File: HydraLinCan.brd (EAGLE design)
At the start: 59.9 x 37 mm, 33 parts, among them CN1 8p-2.54, J1 HYDRABUS_SHIELD_CON_HEADER_2X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, J2 HYDRABUS_SHIELD_CON_HEADER_2X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, J3 HYDRABUS_SHIELD_CON_HEADER_2X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, K1 TS-1188E, U1 SN65HVD233DG4, U2 SN65HVD233DG4, U3 CJ78M05-to252

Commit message: 2 layers parts
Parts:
- moved R5 18.7 mm to (10.2, 24.1), flipped to the bottom
- moved R2 18.4 mm to (14.5, 22.4), turned to 180 degrees
- moved C11 15.8 mm to (19.6, 32.4), flipped to the bottom, turned to 90 degrees
- moved C5 14.5 mm to (10.4, 14.7), flipped to the bottom, turned to 0 degrees
- moved R4 13.7 mm to (10.5, 10.5), flipped to the bottom, turned to 0 degrees
- moved R11 11.0 mm to (48.9, 19.8), turned to 270 degrees
- moved CAN1 10.4 mm to (26.8, 14.4), turned to 270 degrees
- moved R3 9.83 mm to (27.9, 10.0), flipped to the bottom, turned to 180 degrees
- moved R10 9.63 mm to (49.0, 11.4), turned to 270 degrees
- moved R9 9.22 mm to (26.5, 23.5), turned to 180 degrees
- moved J_USB 8.96 mm to (15.1, 3.81)
- moved R6 8.81 mm to (37.0, 14.4), flipped to the bottom, turned to 270 degrees
- moved R8 8.72 mm to (26.7, 10.9), turned to 0 degrees
- moved C12 8.58 mm to (15.2, 18.0), flipped to the bottom, turned to 0 degrees
- moved C10 7.27 mm to (25.7, 23.5), flipped to the bottom, turned to 180 degrees
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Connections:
- net N$10 renamed CAN1_P
- net N$11 renamed CAN2_N
- net N$12 renamed CAN2_P
- net N$9 renamed CAN1_N
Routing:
- net +3V3: track 77.6 -> 123.1 mm, vias 5 -> 4
- net N$1: track 48.5 -> 19.9 mm, vias 2 -> 0
- net N$4: track 46.5 -> 19.3 mm, vias 2 -> 0
- net N$17: track 47.4 -> 21.3 mm, vias 4 -> 0
- net GND: track 41.7 -> 62.3 mm, vias 11 -> 5
- net N$13: track 57.3 -> 37.1 mm, vias 3 -> 2
- net CAN1_N: track 56.9 -> 36.7 mm
- net N$15: track 42.1 -> 60.9 mm, vias 2 -> 0
- net N$21: track 32.7 -> 16.5 mm, vias 3 -> 0
- net N$19: track 20.4 -> 4.43 mm, vias 3 -> 0
- net PA10: track 41.9 -> 57.1 mm, vias 4 -> 0
- net N$16: track 17.6 -> 5.60 mm
- net PB7: track 14.4 -> 4.26 mm, vias 2 -> 0
- net PB5: track 13.1 -> 23.0 mm
- net PA2: track 30.1 -> 20.3 mm, vias 4 -> 0
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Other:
- board text added: "HydraLINCAN 1.2"
- board text removed: "HydraCANLIN Shield 1_1"

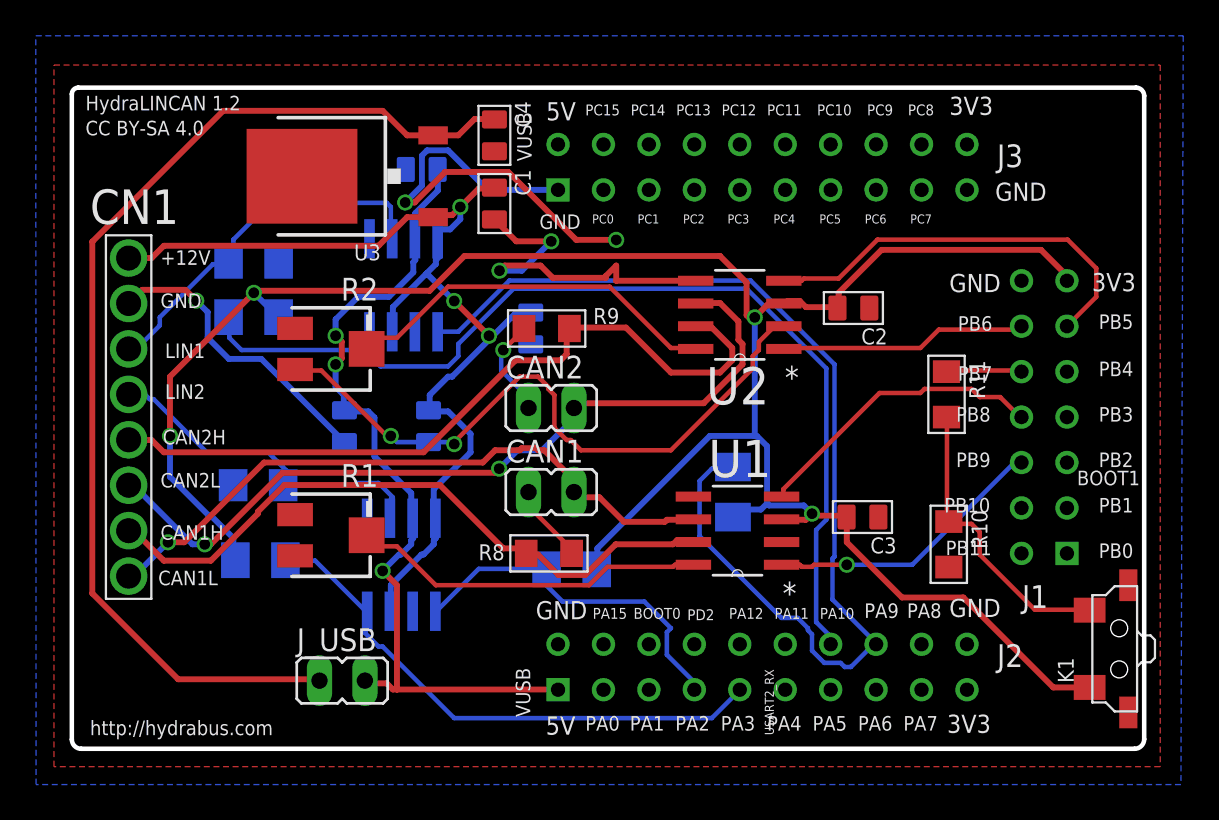
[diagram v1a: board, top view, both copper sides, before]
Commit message: Routing CAN H/L as real diff pairs
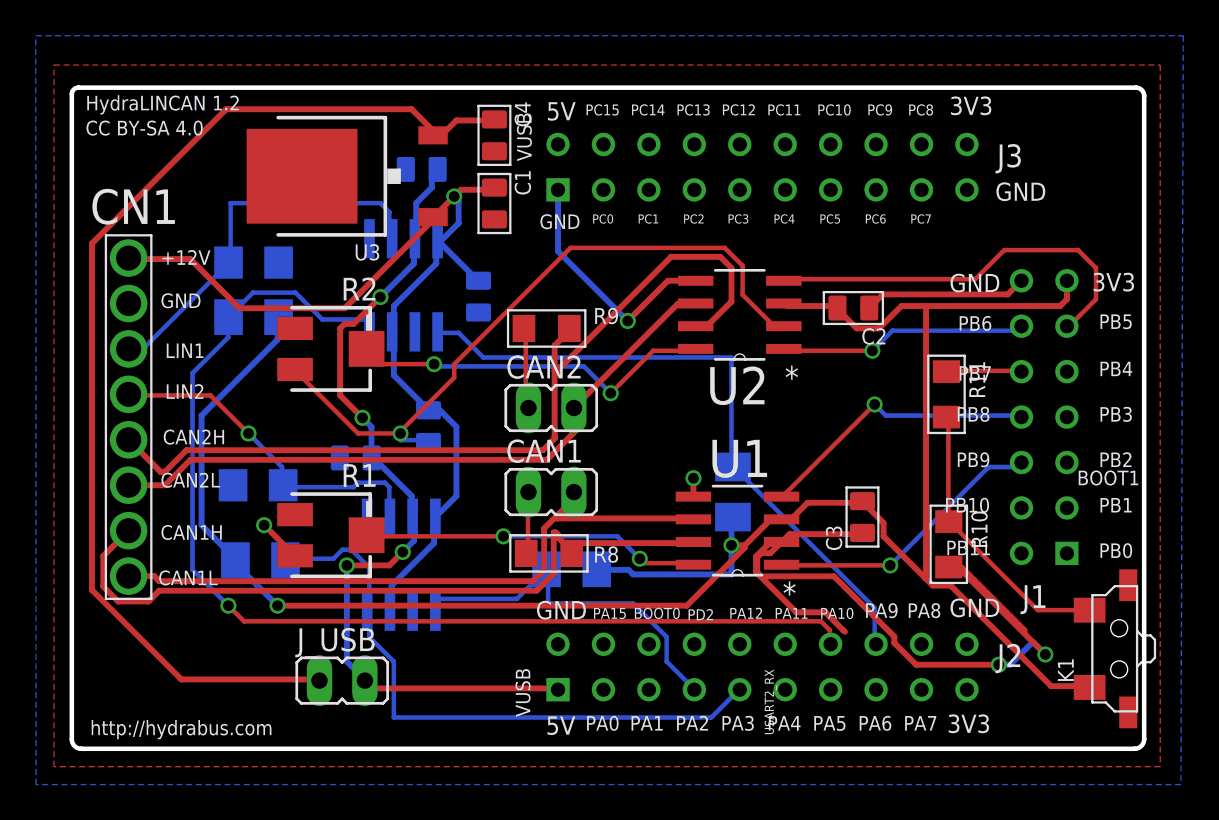
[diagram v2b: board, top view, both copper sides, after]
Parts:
- moved C10 3.42 mm to (22.7, 25.3)
- moved C12 1.89 mm to (15.9, 16.3), turned to 90 degrees
- turned C3 to 180 degrees
- turned R8 to 180 degrees
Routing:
- net PA9: track 61.3 -> 36.4 mm
- net GND: track 62.3 -> 74.4 mm
- net CAN2_N: track 45.5 -> 36.8 mm, vias 2 -> 0
- net CAN2_P: track 42.3 -> 49.1 mm
- net +3V3: track 123.1 -> 117.4 mm, vias 4 -> 2
- net PA10: track 57.1 -> 62.5 mm, vias 0 -> 1
- net CAN1_P: track 37.1 -> 41.6 mm, vias 0 -> 1
- net PA3: track 30.6 -> 34.4 mm
- net +12V: track 59.4 -> 56.5 mm, vias 3 -> 1
- net N$13: track 37.1 -> 38.4 mm, vias 2 -> 1
- net N$16: track 5.60 -> 4.54 mm, vias 1 -> 0
- net N$19: track 4.43 -> 3.48 mm
- net PB8: track 16.8 -> 15.8 mm, vias 0 -> 1
- net N$1: track 19.9 -> 19.0 mm, vias 0 -> 2
- net N$7: track 20.8 -> 21.6 mm
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
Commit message: Silkscreen cleaning
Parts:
- renumbered K1 to UBTN
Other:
- board text added: "CAN1_ADJ"
- board text added: "CAN2_ADJ"

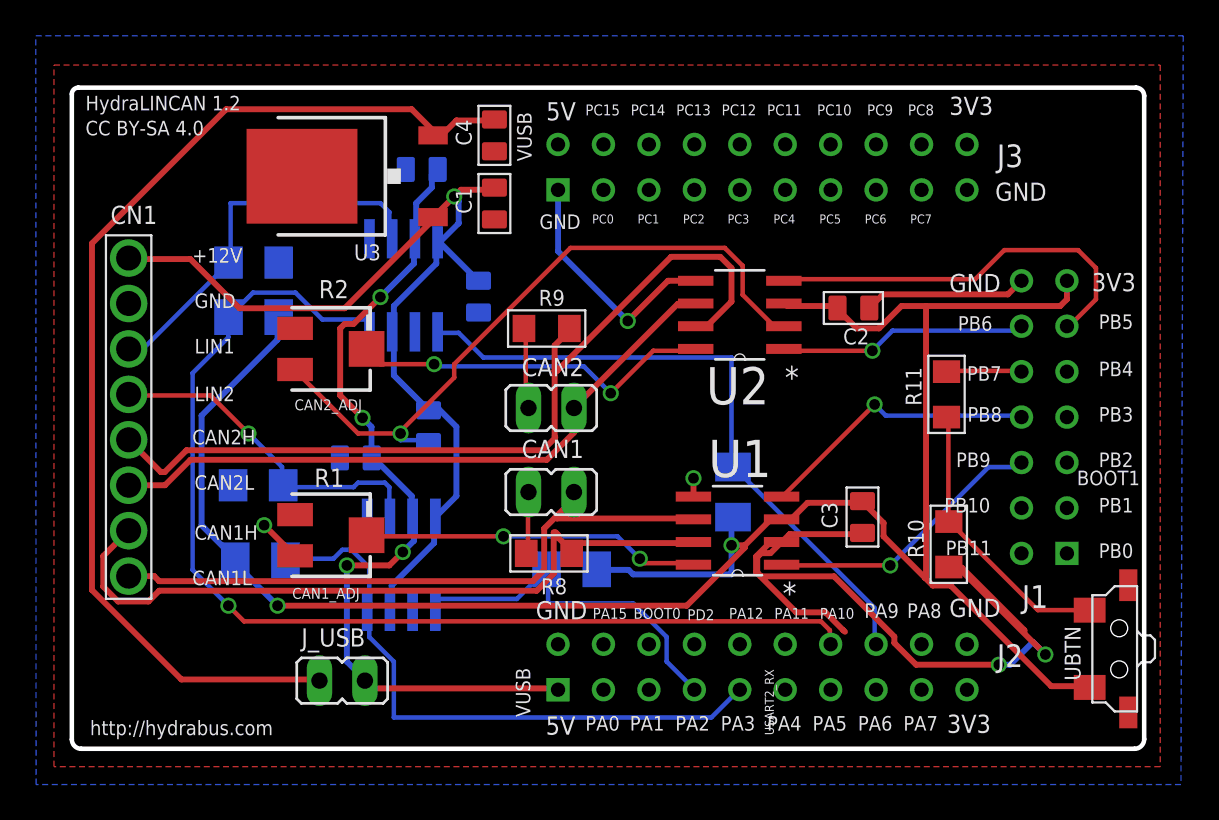
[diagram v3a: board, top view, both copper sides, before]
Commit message: Upgrade LIN transceivers for LIN2.0-2.2A/SAE J2602 and ISO 17984-4 compatibility
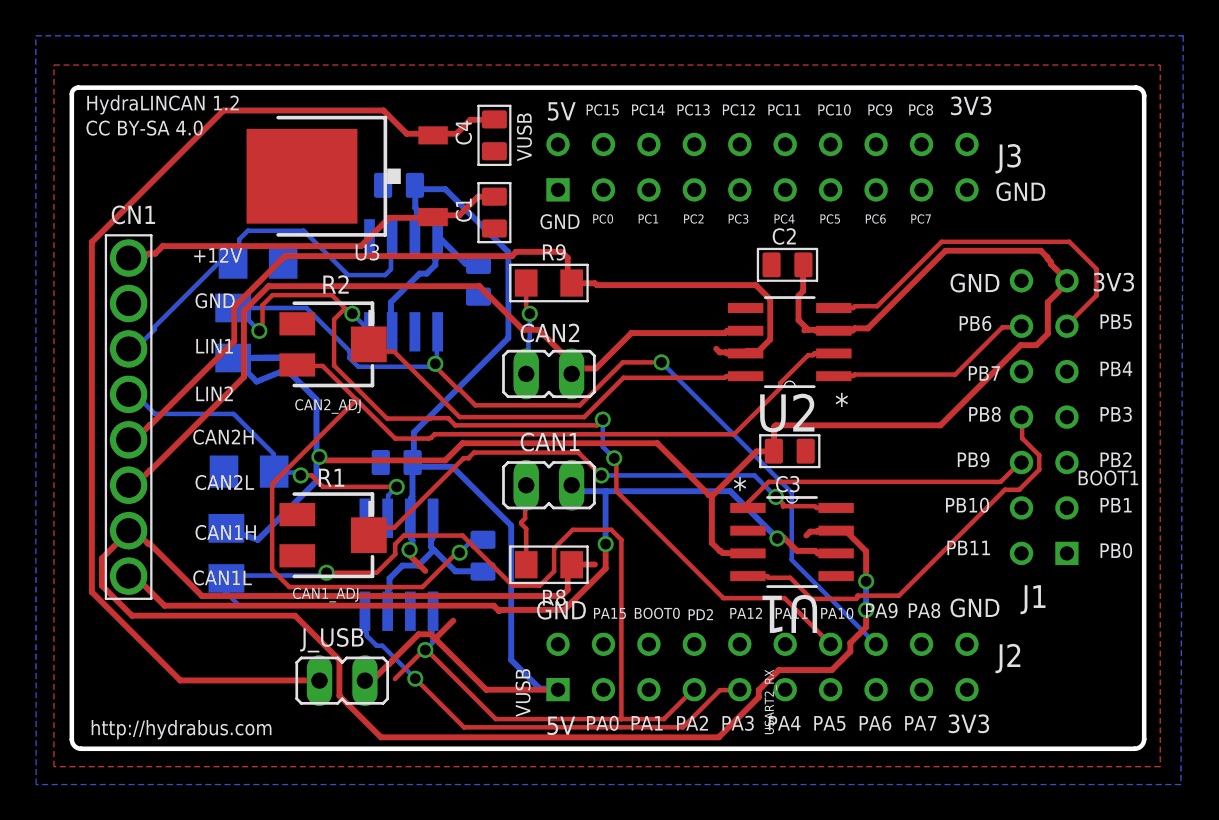
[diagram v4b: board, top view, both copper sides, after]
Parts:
- removed R10, R11: 4k7, Seeed-OPL-Resistor:R1206
- removed R4, R5: 4K7, resistor:M1206
- removed UBTN: TS-1188E, Seeed-OPL-Button:SW4-SMD-7.0X3.5X3.5MM-90D
- LIN1, LIN2: value TJA1020SO8 -> TJA1021SO8
- moved R6 29.3 mm to (9.02, 23.2)
- moved R3 19.3 mm to (8.64, 10.9), turned to 90 degrees
- moved C9 7.85 mm to (23.0, 10.8), turned to 0 degrees
- moved C3 5.48 mm to (40.1, 16.6), turned to 270 degrees
- moved C2 4.40 mm to (40.0, 27.1), turned to 90 degrees
- moved U2 3.18 mm to (40.1, 22.7)
- moved U1 3.11 mm to (40.3, 11.6), turned to 0 degrees
- moved R9 2.54 mm to (26.7, 26.0)
- moved C12 2.30 mm to (18.2, 16.0)
- moved CAN2 1.91 mm to (26.7, 21.0)
- moved C11 1.55 mm to (18.3, 31.5)
- moved C5 0.92 mm to (9.91, 15.5)
- moved C10 0.89 mm to (22.7, 26.2)
- moved R8 0.63 mm to (26.7, 10.3)
- moved C1 0.51 mm to (23.6, 30.0)
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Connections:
- removed net N$21: R10.1, R11.2, UBTN.2
- new net N$10: C10.2, LIN2.3, LIN2.8
- new net N$9: C9.2, LIN1.3, LIN1.8
- net +12V: no longer C10.2, C9.2, LIN1.3, LIN1.8, LIN2.3, LIN2.8
- net +3V3: no longer R4.2, R5.2, UBTN.1
- net GND: no longer R10.2
- net PA10: no longer R5.1
- net PA3: no longer R4.1
- net PB7: no longer R11.1
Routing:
- net GND: track 74.4 -> 0.00 mm, vias 5 -> 0
- net CAN1_P: track 41.6 -> 91.3 mm, vias 1 -> 2
- net PA2: track 20.5 -> 59.0 mm, vias 0 -> 2
- net +12V: track 56.5 -> 21.9 mm, vias 1 -> 0
- net N$13: track 38.4 -> 58.6 mm
- net +3V3: track 117.4 -> 100.4 mm, vias 2 -> 1
- net VCC/2: track 47.2 -> 63.3 mm, vias 4 -> 1
- net N$21: track 15.8 -> 0.00 mm
- net PA9: track 36.4 -> 50.4 mm, vias 0 -> 2
- net CAN1_N: track 36.6 -> 49.2 mm, vias 0 -> 2
- net PA10: track 62.5 -> 50.6 mm, vias 1 -> 4
- net N$1: track 19.0 -> 29.4 mm
- net N$9: track 0.00 -> 10.2 mm
- net N$10: track 0.00 -> 9.48 mm
- net CAN2_N: track 36.8 -> 44.8 mm
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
